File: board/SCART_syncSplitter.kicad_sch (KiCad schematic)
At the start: 33 parts, among them J1 SCART-F, J2 VGA Out, J3 POWER IN, J4 HSync Selector, J5 Audio Out, U1 LMH1981, U2 L7805

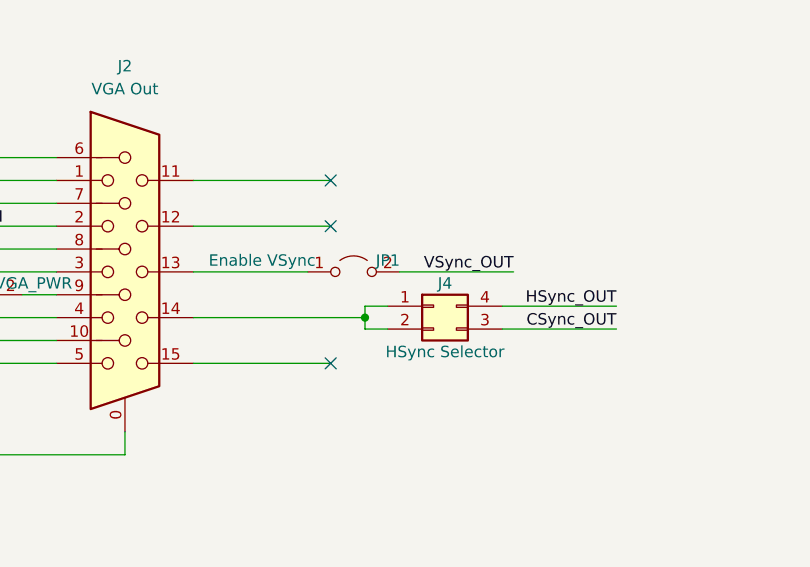
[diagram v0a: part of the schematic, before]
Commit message: Rev 1 of the schematics: invert vsync/hsync pins on VGA
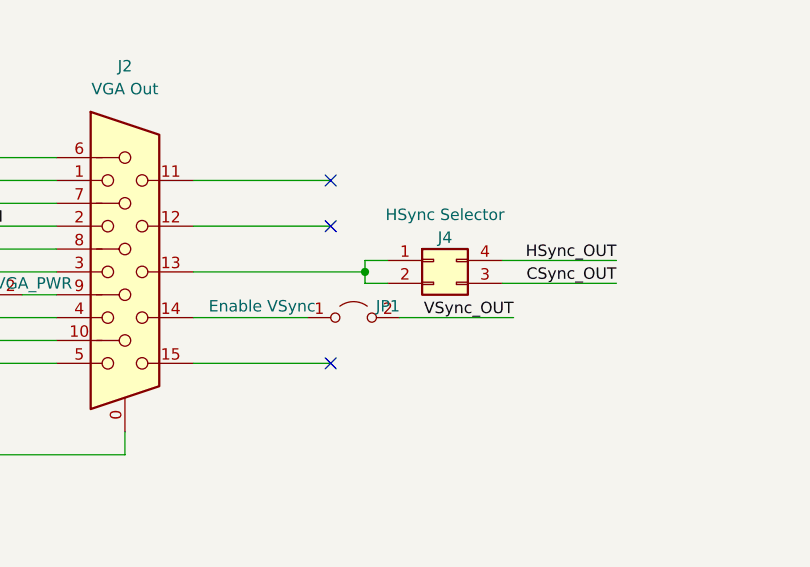
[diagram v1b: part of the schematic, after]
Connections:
- net at J2.13: now also J4.1 (Pin_1), J4.2 (Pin_2); no longer JP1.1 (A)
- new net: J2.14, JP1.1 (A)
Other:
- moved on the sheet: J4, JP1
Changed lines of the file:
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@@
   (paper "A4")
   (title_block
-    (rev "0")
+    (rev "1")
   )
   (junction (at 177.8 139.7) (diameter 0) (color 0 0 0 0)
@@
   (junction (at 218.44 25.4) (diameter 0) (color 0 0 0 0)
   )
-  (junction (at 232.41 137.16) (diameter 0) (color 0 0 0 0)
+  (junction (at 232.41 132.08) (diameter 0) (color 0 0 0 0)
   )
   (junction (at 19.05 127) (diameter 0) (color 0 0 0 0)
@@
     (stroke (width 0) (type default))
   )
-  (wire (pts (xy 213.36 137.16) (xy 232.41 137.16))
+  (wire (pts (xy 213.36 132.08) (xy 232.41 132.08))
     (stroke (width 0) (type default))
   )
@@
     (stroke (width 0) (type default))
   )
-  (wire (pts (xy 236.22 132.08) (xy 248.92 132.08))
+  (wire (pts (xy 236.22 137.16) (xy 248.92 137.16))
     (stroke (width 0) (type default))
   )
@@
     (stroke (width 0) (type default))
   )
-  (wire (pts (xy 234.95 138.43) (xy 232.41 138.43))
+  (wire (pts (xy 234.95 133.35) (xy 232.41 133.35))
     (stroke (width 0) (type default))
   )
@@
     (stroke (width 0) (type default))
   )
-  (wire (pts (xy 247.65 135.89) (xy 260.35 135.89))
+  (wire (pts (xy 247.65 130.81) (xy 260.35 130.81))
     (stroke (width 0) (type default))
   )
@@
     (stroke (width 0) (type default))
   )
-  (wire (pts (xy 247.65 138.43) (xy 260.35 138.43))
+  (wire (pts (xy 247.65 133.35) (xy 260.35 133.35))
     (stroke (width 0) (type default))
   )
@@
     (stroke (width 0) (type default))
   )
-  (wire (pts (xy 232.41 137.16) (xy 232.41 135.89))
+  (wire (pts (xy 232.41 132.08) (xy 232.41 130.81))
     (stroke (width 0) (type default))
   )
@@
     (stroke (width 0) (type default))
   )
-  (wire (pts (xy 232.41 138.43) (xy 232.41 137.16))
+  (wire (pts (xy 232.41 133.35) (xy 232.41 132.08))
     (stroke (width 0) (type default))
   )
@@
     (stroke (width 0) (type default))
   )
-  (wire (pts (xy 232.41 135.89) (xy 234.95 135.89))
+  (wire (pts (xy 232.41 130.81) (xy 234.95 130.81))
     (stroke (width 0) (type default))
   )
@@
     (stroke (width 0) (type default))
   )
-  (wire (pts (xy 213.36 132.08) (xy 226.06 132.08))
+  (wire (pts (xy 213.36 137.16) (xy 226.06 137.16))
     (stroke (width 0) (type default))
   )
@@
     (effects (font (size 1.27 1.27)) (justify left bottom))
   )
-  (label "VSync_OUT" (at 248.92 132.08 180) (fields_autoplaced)
+  (label "VSync_OUT" (at 248.92 137.16 180) (fields_autoplaced)
     (effects (font (size 1.27 1.27)) (justify right bottom))
   )
-  (label "CSync_OUT" (at 260.35 138.43 180) (fields_autoplaced)
+  (label "CSync_OUT" (at 260.35 133.35 180) (fields_autoplaced)
     (effects (font (size 1.27 1.27)) (justify right bottom))
   )
@@
     (effects (font (size 1.27 1.27)) (justify left bottom))
   )
-  (label "HSync_OUT" (at 260.35 135.89 180) (fields_autoplaced)
+  (label "HSync_OUT" (at 260.35 130.81 180) (fields_autoplaced)
     (effects (font (size 1.27 1.27)) (justify right bottom))
   )
@@
     )
   )
-  (symbol (lib_id "Connector_Generic:Conn_02x02_Counter_Clockwise") (at 240.03 135.89 0) (unit 1)
-    (in_bom yes) (on_board yes) (dnp no)
-    (property "Reference" "J4" (at 241.3 133.35 0)
-      (effects (font (size 1.27 1.27)))
-    )
-    (property "Value" "HSync Selector" (at 241.3 140.97 0)
-      (effects (font (size 1.27 1.27)))
-    )
-    (property "Footprint" "Connector_PinHeader_2.54mm:PinHeader_2x02_P2.54mm_Vertical" (at 240.03 135.89 0)
-      (effects (font (size 1.27 1.27)) hide)
-    )
-    (property "Datasheet" "~" (at 240.03 135.89 0)
+  (symbol (lib_id "Connector_Generic:Conn_02x02_Counter_Clockwise") (at 240.03 130.81 0) (unit 1)
+    (in_bom yes) (on_board yes) (dnp no)
+    (property "Reference" "J4" (at 241.3 128.27 0)
+      (effects (font (size 1.27 1.27)))
+    )
+    (property "Value" "HSync Selector" (at 241.3 125.73 0)
+      (effects (font (size 1.27 1.27)))
+    )
+    (property "Footprint" "Connector_PinHeader_2.54mm:PinHeader_2x02_P2.54mm_Vertical" (at 240.03 130.81 0)
+      (effects (font (size 1.27 1.27)) hide)
+    )
+    (property "Datasheet" "~" (at 240.03 130.81 0)
       (effects (font (size 1.27 1.27)) hide)
     )
@@
     )
   )
-  (symbol (lib_id "Jumper:Jumper_2_Open") (at 231.14 132.08 0) (unit 1)
-    (in_bom yes) (on_board yes) (dnp no)
-    (property "Reference" "JP1" (at 234.95 130.81 0)
-      (effects (font (size 1.27 1.27)))
-    )
-    (property "Value" "Enable VSync" (at 220.98 130.81 0)
-      (effects (font (size 1.27 1.27)))
-    )
-    (property "Footprint" "Connector_PinHeader_2.54mm:PinHeader_1x02_P2.54mm_Vertical" (at 231.14 132.08 0)
-      (effects (font (size 1.27 1.27)) hide)
-    )
-    (property "Datasheet" "~" (at 231.14 132.08 0)
-      (effects (font (size 1.27 1.27)) hide)
-    )
+  (symbol (lib_id "Jumper:Jumper_2_Open") (at 231.14 137.16 0) (unit 1)
+    (in_bom yes) (on_board yes) (dnp no)
+    (property "Reference" "JP1" (at 234.95 135.89 0)
+      (effects (font (size 1.27 1.27)))
+    )
+    (property "Value" "Enable VSync" (at 220.98 135.89 0)
+      (effects (font (size 1.27 1.27)))
+    )
+    (property "Footprint" "Connector_PinHeader_2.54mm:PinHeader_1x02_P2.54mm_Vertical" (at 231.14 137.16 0)
+      (effects (font (size 1.27 1.27)) hide)
+    )
+    (property "Datasheet" "~" (at 231.14 137.16 0)
+      (effects (font (size 1.27 1.27)) hide)
+    )

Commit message: Update project for rev.1 board
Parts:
- C1: value 570pF -> 560pF
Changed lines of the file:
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@@
       (effects (font (size 1.27 1.27)) (justify left))
     )
-    (property "Value" "570pF" (at 50.8 26.6763 0)
+    (property "Value" "560pF" (at 50.8 26.6763 0)
       (effects (font (size 1.27 1.27)) (justify left))
     )
